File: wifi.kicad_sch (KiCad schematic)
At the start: 3 parts, among them J3 U_FL-R-SMT-1, U19 LBEE5PK2AE

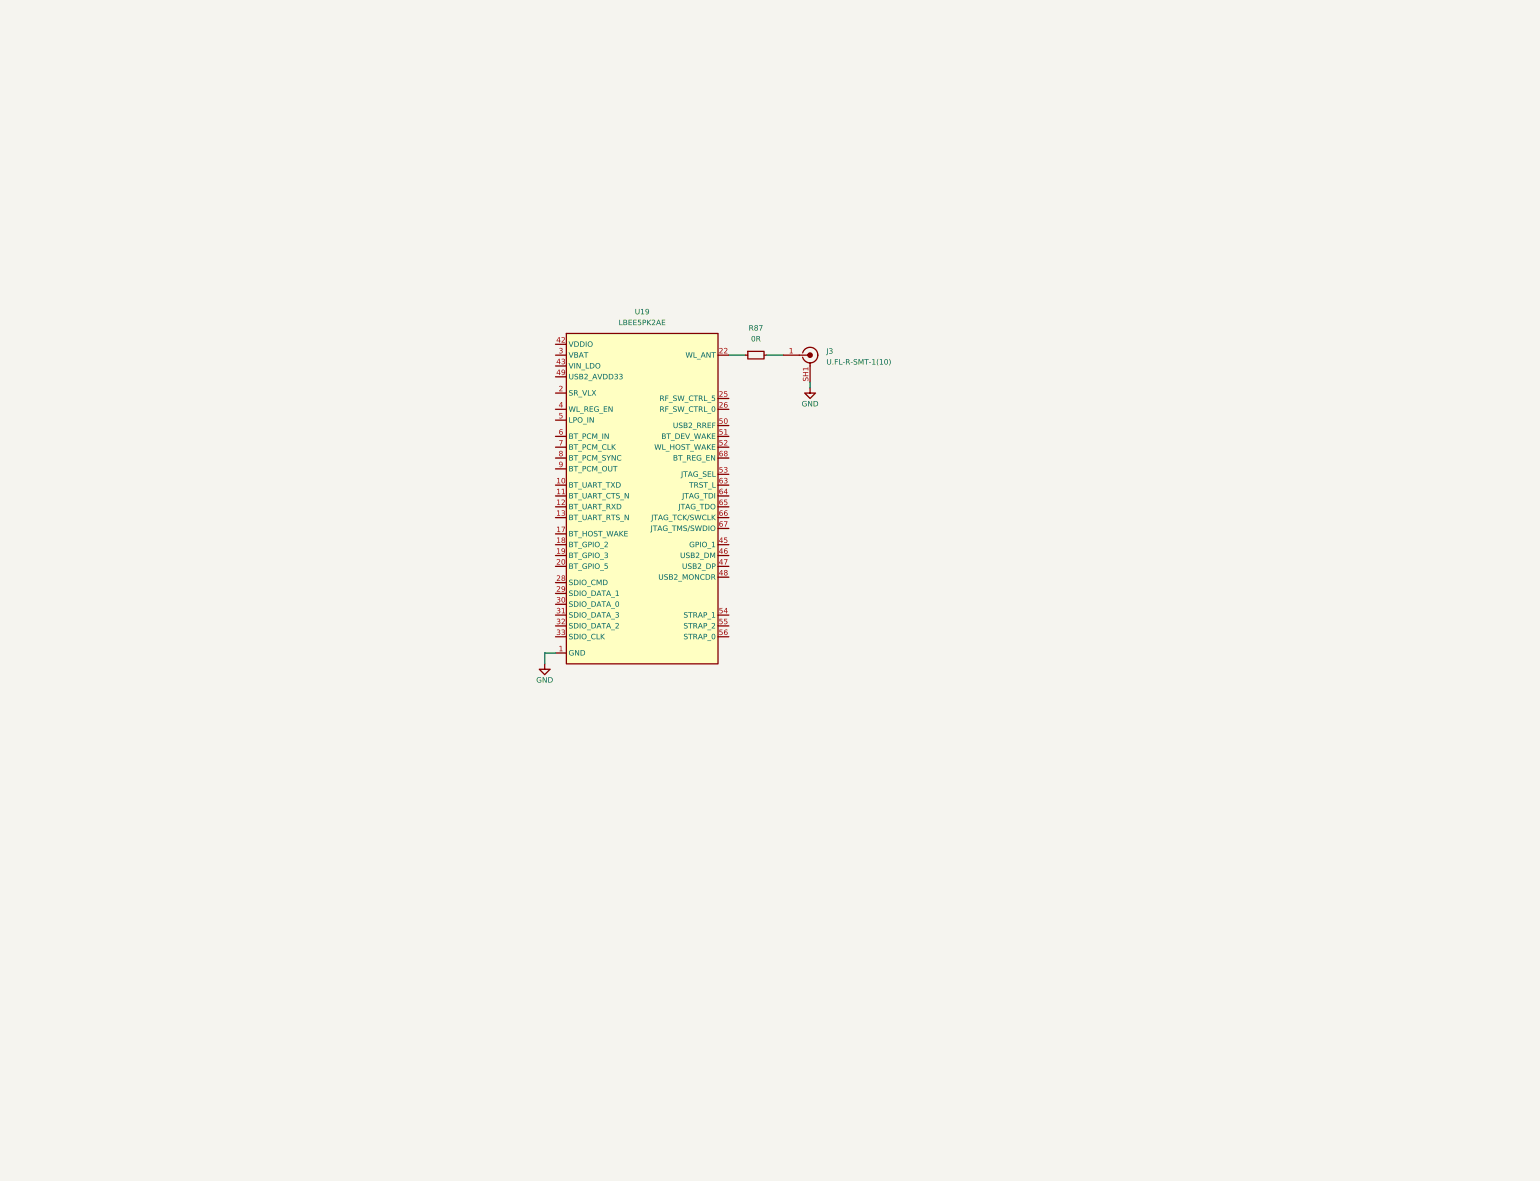
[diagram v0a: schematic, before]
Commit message: [#54178] Add WiFi module with adjacent components
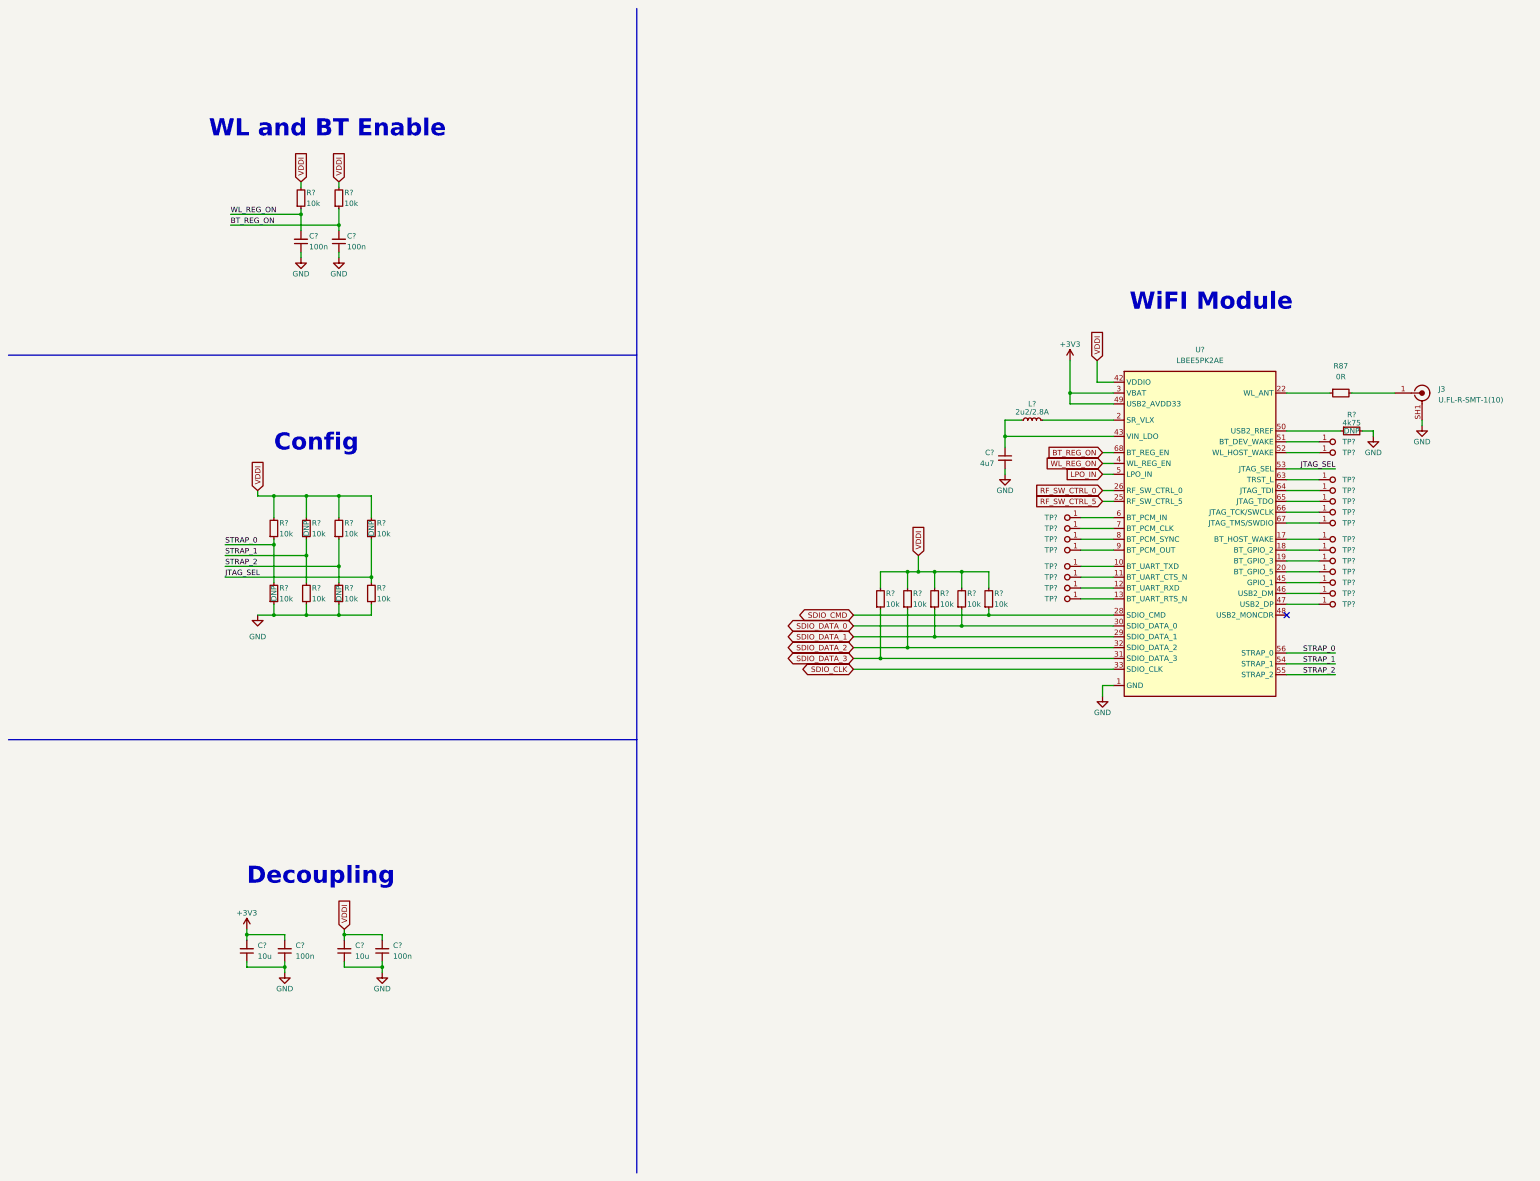
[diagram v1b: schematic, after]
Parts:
- removed U19: LBEE5PK2AE, antmicro-footprints:LBEE5PK2AE, symbol antmicroInterfaceModules:LBEE5PK2AE
- added C? (x2): C_10u_0402, antmicro-footprints:C_0402_1005Metric, symbol antmicroCapacitors0402:C_10u_0402
- added C? (x4): C_100n_0402, antmicro-footprints:C_0402_1005Metric, symbol antmicroCapacitors0402:C_100n_0402
- added C?: C_4u7_0402, antmicro-footprints:C_0402_1005Metric, symbol antmicroCapacitors0402:C_4u7_0402
- added L?: L_2u2_2.8A_1008, antmicro-footprints:L_1008_2520Metric, symbol antmicroFixedInductors:L_2u2_2.8A_1008
- added R? (x15): R_10k_0402, antmicro-footprints:R_0402_1005Metric, symbol antmicroResistors0402:R_10k_0402
- added R?: R_4k75_0.5%_0402, antmicro-footprints:R_0402_1005Metric, symbol antmicroResistors0402:R_4k75_0.5%_0402
- added TP? (x22): TP_0.75mm_SMD, antmicro-footprints:TP_SMD_0.75mm, symbol antmicroTestPoints:TP_0.75mm_SMD
- added U?: LBEE5PK2AE, antmicro-footprints:LBEE5PK2AE, symbol antmicroInterfaceModules:LBEE5PK2AE
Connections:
- net GND: now also C?.1, C?.1, C?.1, C?.1, C?.1, C?.1, C?.2, R?.1, R?.1, R?.1, R?.1, R?.2, U?.1 (GND), U?.14 (GND), U?.16 (GND), U?.21 (GND), U?.23 (GND), U?.24 (GND), U?.27 (GND), U?.34 (GND), U?.41 (GND), U?.57 (GND), U?.69 (GND), U?.70 (GND), U?.71 (GND), U?.72 (GND), U?.73 (GND), U?.74 (GND), U?.75 (GND), U?.76 (GND), U?.77 (GND)
- net at R87.1: now also U?.22 (WL_ANT)
- new net: TP?.1, U?.12 (BT_UART_RXD)
- new net: TP?.1, U?.47 (USB2_DP)
- new net: TP?.1, U?.51 (BT_DEV_WAKE)
- new net: TP?.1, U?.63 (TRST_L)
- new net: TP?.1, U?.7 (BT_PCM_CLK)
- new net: C?.1, L?.1, U?.43 (VIN_LDO)
- new net: L?.2, U?.2 (SR_VLX)
- new net: TP?.1, U?.65 (JTAG_TDO)
- new net: TP?.1, U?.46 (USB2_DM)
- new net: TP?.1, U?.10 (BT_UART_TXD)
- new net: TP?.1, U?.11 (BT_UART_CTS_N)
- new net: TP?.1, U?.13 (BT_UART_RTS_N)
- new net: U?.15 (NC), U?.35 (NC), U?.36 (NC), U?.37 (NC), U?.38 (NC), U?.39 (NC), U?.40 (NC), U?.44 (NC), U?.58 (NC), U?.59 (NC), U?.60 (NC), U?.61 (NC), U?.62 (NC)
- new net: TP?.1, U?.17 (BT_HOST_WAKE)
- new net: TP?.1, U?.18 (BT_GPIO_2)
- new net: TP?.1, U?.19 (BT_GPIO_3)
- new net: TP?.1, U?.20 (BT_GPIO_5)
- new net: TP?.1, U?.45 (GPIO_1)
- new net: R?.1, U?.50 (USB2_RREF)
- new net: TP?.1, U?.52 (WL_HOST_WAKE)
- new net: TP?.1, U?.6 (BT_PCM_IN)
- new net: TP?.1, U?.64 (JTAG_TDI)
- new net: TP?.1, U?.66 (JTAG_TCK/SWCLK)
- new net: TP?.1, U?.67 (JTAG_TMS/SWDIO)
- new net: TP?.1, U?.8 (BT_PCM_SYNC)
- new net: TP?.1, U?.9 (BT_PCM_OUT)
- new net +3V3: C?.2, C?.2, U?.3 (VBAT), U?.49 (USB2_AVDD33)
- new net BT_REG_ON: C?.2, R?.1, U?.68 (BT_REG_EN)
- new net JTAG_SEL: R?.1, R?.2, U?.53 (JTAG_SEL)
- new net LPO_IN: U?.5 (LPO_IN)
- new net RF_SW_CTRL_0: U?.26 (RF_SW_CTRL_0)
- new net RF_SW_CTRL_5: U?.25 (RF_SW_CTRL_5)
- new net SDIO_CLK: U?.33 (SDIO_CLK)
- new net SDIO_CMD: R?.1, U?.28 (SDIO_CMD)
- new net SDIO_DATA_0: R?.1, U?.30 (SDIO_DATA_0)
- new net SDIO_DATA_1: R?.1, U?.29 (SDIO_DATA_1)
- new net SDIO_DATA_2: R?.1, U?.32 (SDIO_DATA_2)
- new net SDIO_DATA_3: R?.1, U?.31 (SDIO_DATA_3)
- new net STRAP_0: R?.1, R?.2, U?.56 (STRAP_0)
- new net STRAP_1: R?.1, R?.2, U?.54 (STRAP_1)
- new net STRAP_2: R?.1, R?.2, U?.55 (STRAP_2)
- new net VDDI: C?.2, C?.2, R?.2, R?.2, R?.2, R?.2, R?.2, R?.2, R?.2, R?.2, R?.2, R?.2, R?.2, U?.42 (VDDIO)
- new net WL_REG_ON: C?.2, R?.1, U?.4 (WL_REG_EN)
- no-connect marks 0 -> 1
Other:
- note added: "Config"
- note added: "Decoupling"
- note added: "WL and BT Enable"
- note added: "WiFI Module"
- moved on the sheet: J3, R87

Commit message: [#54178] Add UART to WiFi module
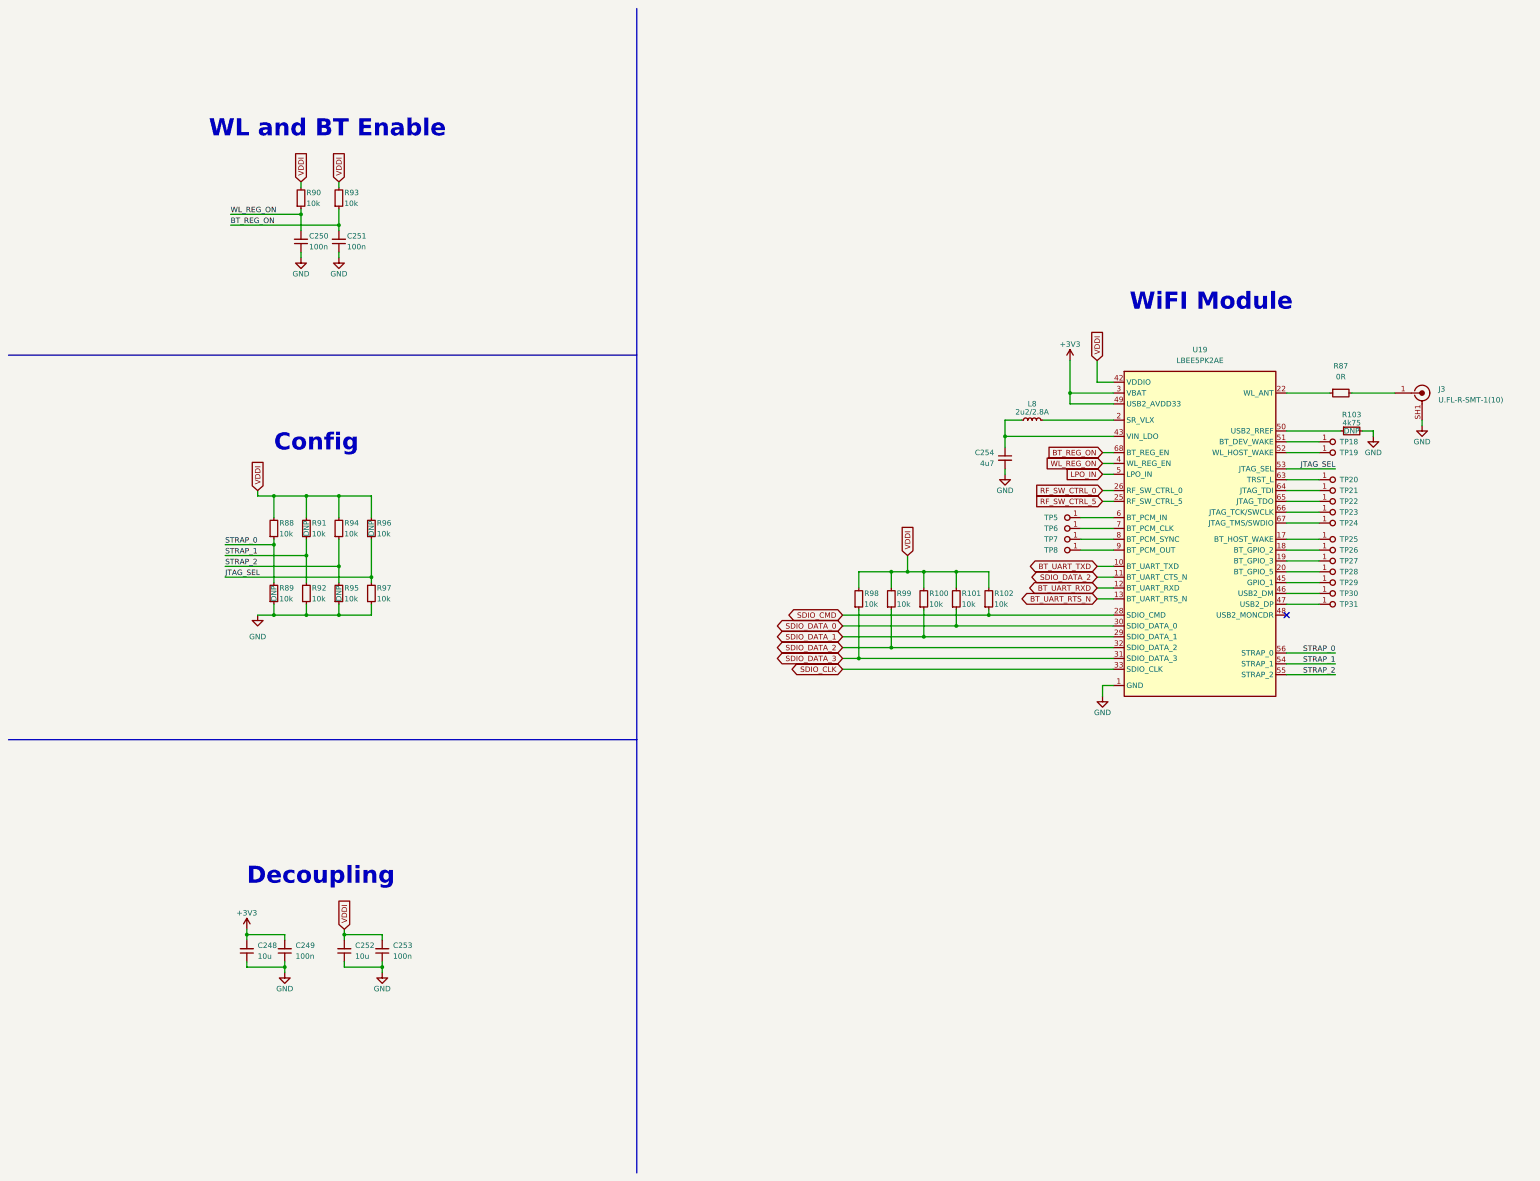
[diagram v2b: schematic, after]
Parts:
- removed TP? (x4): TP_0.75mm_SMD, antmicro-footprints:TP_SMD_0.75mm, symbol antmicroTestPoints:TP_0.75mm_SMD
- gave numbers to parts that had none: 43
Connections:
- net SDIO_DATA_2: now also U19.11 (BT_UART_CTS_N)
- net BT_UART_RXD: now reaches U19.12 (BT_UART_RXD)
- net BT_UART_TXD: now reaches U19.10 (BT_UART_TXD)
- net BT_UART_RTS_N: now reaches U19.13 (BT_UART_RTS_N)
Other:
- moved on the sheet: R100, R101, R98, R99

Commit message: [#54178] Add sleep clock
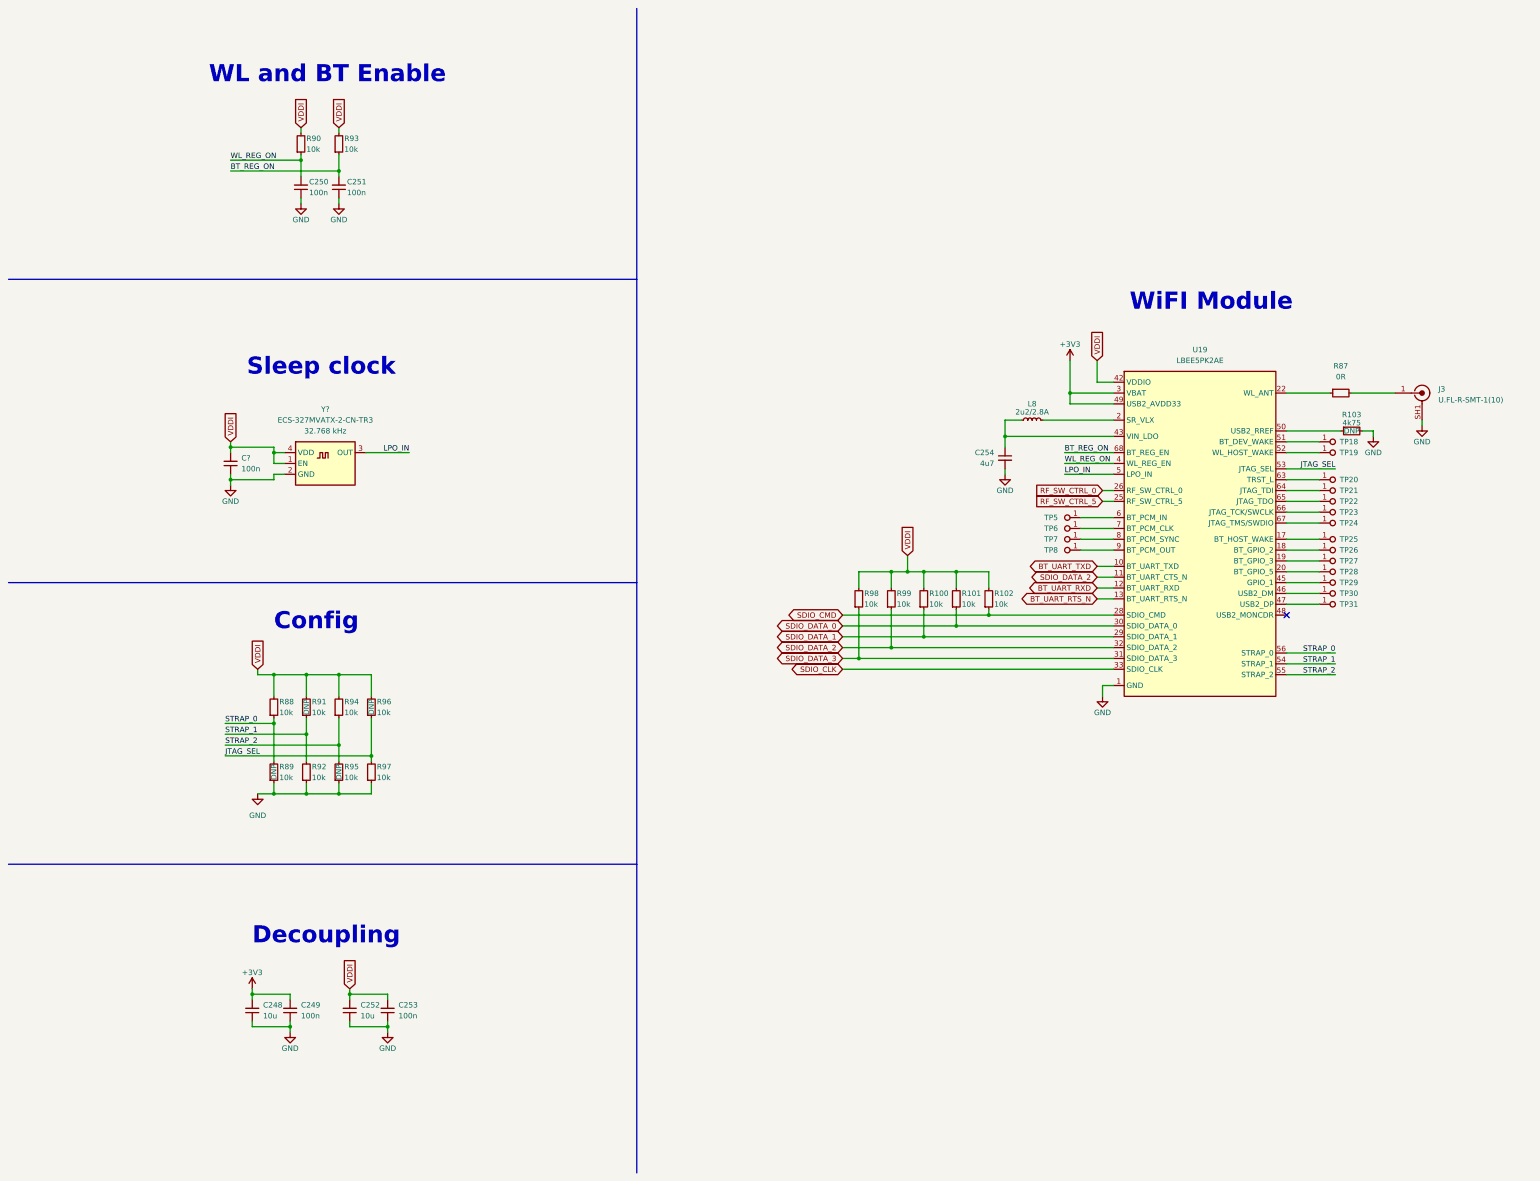
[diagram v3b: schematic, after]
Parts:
- added C?: C_100n_0402, antmicro-footprints:C_0402_1005Metric, symbol antmicroCapacitors0402:C_100n_0402
- added Y?: Oscillator_32.768kHz_ECS_2520MV, antmicro-footprints:Oscillator_SMD_ECS_2520MV_2.5x2mm, symbol antmicroOscillators:Oscillator_32.768kHz_ECS_2520MV
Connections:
- net GND: now also C?.1, Y?.2 (GND)
- net LPO_IN: now also Y?.3 (OUT)
- net VDDI: now also C?.2, Y?.1 (EN), Y?.4 (VDD)
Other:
- note added: "Sleep clock"
- moved on the sheet: C248, C249, C250, C251, C252, C253, R88, R89, R90, R91, R92, R93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
